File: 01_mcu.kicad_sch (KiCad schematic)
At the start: 3 parts, among them J4 UART, J5 SWD

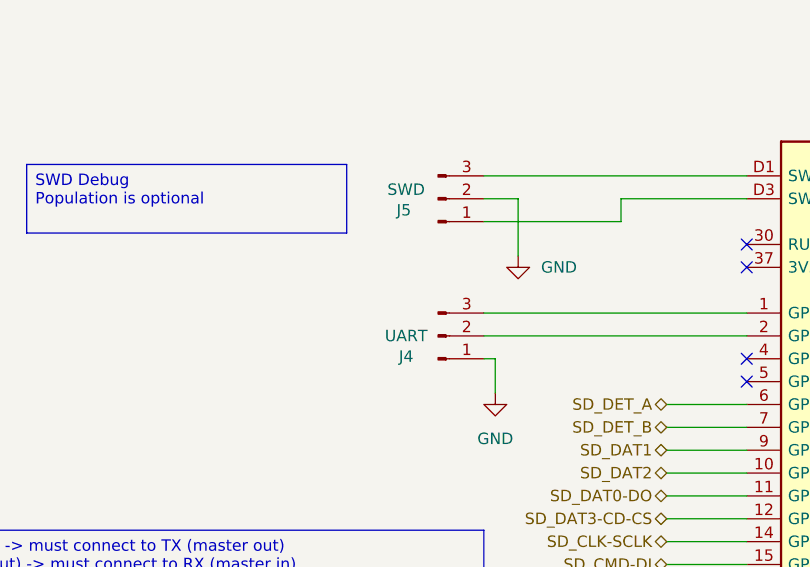
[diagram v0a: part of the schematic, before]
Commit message: Connect both USB data lines again, checked everything with datasheets again
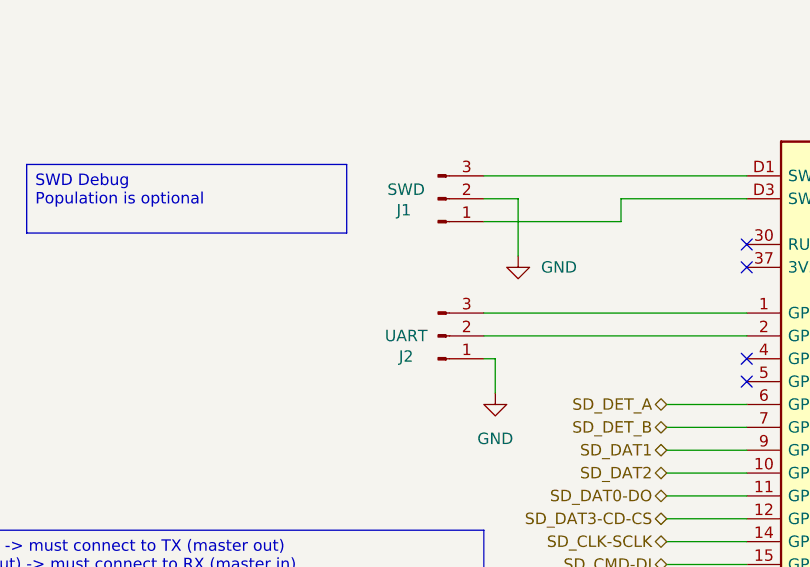
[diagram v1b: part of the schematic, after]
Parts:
- renumbered J5 to J1, J4 to J2
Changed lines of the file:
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@@
 		(dnp no)
 		(fields_autoplaced yes)
-		(property "Reference" "#PWR014"
+		(property "Reference" "#PWR07"
 			(at 158.75 146.05 0)
 			(effects
@@
 			(project ""
 				(path "/ec954637-2a8b-4662-b4a1-f88107f11cb0/8ebc337b-62e9-431a-9c7d-4f5ee75e8f92"
-					(reference "#PWR014")
+					(reference "#PWR07")
 					(unit 1)
 				)
@@
 		(on_board yes)
 		(dnp no)
-		(property "Reference" "J5"
+		(property "Reference" "J1"
 			(at 97.79 71.12 0)
 			(effects
@@
 			(project "ZEReader-Pico"
 				(path "/ec954637-2a8b-4662-b4a1-f88107f11cb0/8ebc337b-62e9-431a-9c7d-4f5ee75e8f92"
-					(reference "J5")
+					(reference "J1")
 					(unit 1)
 				)
@@
 		(on_board yes)
 		(dnp no)
-		(property "Reference" "J4"
+		(property "Reference" "J2"
 			(at 98.044 87.376 0)
 			(effects
@@
 			(project ""
 				(path "/ec954637-2a8b-4662-b4a1-f88107f11cb0/8ebc337b-62e9-431a-9c7d-4f5ee75e8f92"
-					(reference "J4")
+					(reference "J2")
 					(unit 1)
 				)
@@
 		(dnp no)
 		(fields_autoplaced yes)
-		(property "Reference" "#PWR022"
+		(property "Reference" "#PWR06"
 			(at 110.49 82.55 0)
 			(effects
@@
 			(project ""
 				(path "/ec954637-2a8b-4662-b4a1-f88107f11cb0/8ebc337b-62e9-431a-9c7d-4f5ee75e8f92"
-					(reference "#PWR022")
+					(reference "#PWR06")
 					(unit 1)
 				)
@@
 		(dnp no)
 		(fields_autoplaced yes)
-		(property "Reference" "#PWR012"
+		(property "Reference" "#PWR05"
 			(at 107.95 97.79 0)
 			(effects
@@
 			(project ""
 				(path "/ec954637-2a8b-4662-b4a1-f88107f11cb0/8ebc337b-62e9-431a-9c7d-4f5ee75e8f92"
-					(reference "#PWR012")
+					(reference "#PWR05")
 					(unit 1)
 				)
@@
 		(on_board yes)
 		(dnp no)
-		(property "Reference" "#PWR027"
+		(property "Reference" "#PWR08"
 			(at 163.83 41.91 0)
 			(effects
@@
 			(project ""
 				(path "/ec954637-2a8b-4662-b4a1-f88107f11cb0/8ebc337b-62e9-431a-9c7d-4f5ee75e8f92"
-					(reference "#PWR027")
-					(unit 1)
-				)
+					(reference "#PWR08")
+					(unit 1)
+				)

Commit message: Reworked the PCB after review
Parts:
- removed J1: SWD, Connector_PinHeader_2.54mm:PinHeader_1x03_P2.54mm_Vertical, symbol Connector:Conn_01x03_Pin
- added J2: Conn_02x05_Odd_Even, Connector_PinHeader_1.27mm:PinHeader_2x05_P1.27mm_Vertical_SMD, symbol Connector_Generic:Conn_02x05_Odd_Even
- renumbered J2 to J1
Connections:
- net GND: now also J2.3 (Pin_3), J2.5 (Pin_5), J2.9 (Pin_9)
- net at A1.D3 (SWDIO): now also J2.2 (Pin_2)
- net at A1.D1 (SWCLK): now also J2.4 (Pin_4)
- net SD_DET_A: no longer names the net of A1.6 (GPIO4)
- no-connect marks 12 -> 18
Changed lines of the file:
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@@
 	(text_box "SWD Debug\nPopulation is optional"
 		(exclude_from_sim no)
-		(at 55.88 66.04 0)
+		(at 52.07 62.23 0)
 		(size 35.56 7.62)
 		(margins 0.9525 0.9525 0.9525 0.9525)
@@
 			(justify left top)
 		)
+	)
+	(junction
+		(at 92.71 69.85)
+		(diameter 0)
+		(color 0 0 0 0)
+	)
+	(junction
+		(at 92.71 74.93)
+		(diameter 0)
+		(color 0 0 0 0)
 	)
 	(junction
@@
 	)
 	(no_connect
+		(at 135.89 92.71)
+	)
+	(no_connect
+		(at 111.76 69.85)
+	)
+	(no_connect
+		(at 111.76 74.93)
+	)
+	(no_connect
 		(at 135.89 125.73)
 	)
 	(no_connect
+		(at 99.06 72.39)
+	)
+	(no_connect
 		(at 135.89 90.17)
 	)
 	(no_connect
+		(at 99.06 64.77)
+	)
+	(no_connect
 		(at 135.89 74.93)
 	)
@@
 	)
 	(no_connect
+		(at 111.76 72.39)
+	)
+	(no_connect
 		(at 135.89 77.47)
 	)
@@
 	(wire
 		(pts
+			(xy 99.06 69.85) (xy 92.71 69.85)
+		)
+		(stroke
+			(width 0)
+			(type default)
+		)
+	)
+	(wire
+		(pts
 			(xy 181.61 115.57) (xy 189.23 115.57)
 		)
@@
 	(wire
 		(pts
-			(xy 110.49 76.2) (xy 110.49 69.85)
+			(xy 92.71 77.47) (xy 92.71 74.93)
+		)
+		(stroke
+			(width 0)
+			(type default)
+		)
+	)
+	(wire
+		(pts
+			(xy 92.71 69.85) (xy 92.71 67.31)
 		)
 		(stroke
@@
 	(wire
 		(pts
-			(xy 106.68 72.39) (xy 121.92 72.39)
+			(xy 135.89 67.31) (xy 111.76 67.31)
 		)
 		(stroke
@@
 	(wire
 		(pts
-			(xy 106.68 67.31) (xy 135.89 67.31)
-		)
-		(stroke
-			(width 0)
-			(type default)
-		)
-	)
-	(wire
-		(pts
 			(xy 181.61 69.85) (xy 190.5 69.85)
 		)
@@
 	(wire
 		(pts
+			(xy 99.06 67.31) (xy 92.71 67.31)
+		)
+		(stroke
+			(width 0)
+			(type default)
+		)
+	)
+	(wire
+		(pts
 			(xy 163.83 45.72) (xy 163.83 59.69)
 		)
@@
 	(wire
 		(pts
-			(xy 110.49 69.85) (xy 106.68 69.85)
-		)
-		(stroke
-			(width 0)
-			(type default)
-		)
-	)
-	(wire
-		(pts
 			(xy 127 115.57) (xy 135.89 115.57)
 		)
@@
 	(wire
 		(pts
+			(xy 92.71 69.85) (xy 92.71 74.93)
+		)
+		(stroke
+			(width 0)
+			(type default)
+		)
+	)
+	(wire
+		(pts
 			(xy 153.67 38.1) (xy 153.67 59.69)
 		)
@@
 	(wire
 		(pts
-			(xy 127 92.71) (xy 135.89 92.71)
+			(xy 92.71 74.93) (xy 99.06 74.93)
 		)
 		(stroke
@@
 	(wire
 		(pts
-			(xy 121.92 69.85) (xy 121.92 72.39)
+			(xy 111.76 64.77) (xy 121.92 64.77)
+		)
+		(stroke
+			(width 0)
+			(type default)
+		)
+	)
+	(wire
+		(pts
+			(xy 121.92 64.77) (xy 121.92 69.85)
 		)
 		(stroke
@@
 		(shape input)
 		(at 127 118.11 180)
-		(effects
-			(font
-				(size 1.27 1.27)
-			)
-			(justify right)
-		)
-	)
-	(hierarchical_label "SD_DET_A"
-		(shape bidirectional)
-		(at 127 92.71 180)
 		(effects
 			(font
@@
 	(symbol
 		(lib_id "Connector:Conn_01x03_Pin")
-		(at 101.6 69.85 0)
+		(at 101.6 85.09 0)
 		(mirror x)
 		(unit 1)
@@
 		(dnp no)
 		(property "Reference" "J1"
-			(at 97.79 71.12 0)
-			(effects
-				(font
-					(size 1.27 1.27)
-				)
-			)
-		)
-		(property "Value" "SWD"
-			(at 98.044 68.834 0)
-			(effects
-				(font
-					(size 1.27 1.27)
-				)
-			)
-		)
-		(property "Footprint" "Connector_PinHeader_2.54mm:PinHeader_1x03_P2.54mm_Vertical"
-			(at 101.6 69.85 0)
-			(effects
-				(font
-					(size 1.27 1.27)
-				)
-				(hide yes)
-			)
-		)
-		(property "Datasheet" "~"
-			(at 101.6 69.85 0)
-			(effects
-				(font
-					(size 1.27 1.27)
-				)
-				(hide yes)
-			)
-		)
-		(property "Description" "Generic connector, single row, 01x03, script generated"
-			(at 101.6 69.85 0)
-			(effects
-				(font
-					(size 1.27 1.27)
-				)
-				(hide yes)
-			)
-		)
-		(pin "1"
-		)
-		(pin "3"
-		)
-		(pin "2"
-		)
-		(instances
-			(project "ZEReader-Pico"
-				(path "/ec954637-2a8b-4662-b4a1-f88107f11cb0/8ebc337b-62e9-431a-9c7d-4f5ee75e8f92"
-					(reference "J1")
-					(unit 1)
-				)
-			)
-		)
-	)
-	(symbol
-		(lib_id "Connector:Conn_01x03_Pin")
-		(at 101.6 85.09 0)
-		(mirror x)
-		(unit 1)
-		(exclude_from_sim no)
-		(in_bom yes)
-		(on_board yes)
-		(dnp no)
-		(property "Reference" "J2"
 			(at 98.044 87.376 0)
 			(effects
@@
 			(project ""
 				(path "/ec954637-2a8b-4662-b4a1-f88107f11cb0/8ebc337b-62e9-431a-9c7d-4f5ee75e8f92"
-					(reference "J2")
+					(reference "J1")
 					(unit 1)
 				)
@@
 	)
 	(symbol
-		(lib_id "power:GND")
-		(at 110.49 76.2 0)
+		(lib_id "Connector_Generic:Conn_02x05_Odd_Even")
+		(at 104.14 69.85 0)
 		(unit 1)
 		(exclude_from_sim no)
@@
 		(dnp no)
 		(fields_autoplaced yes)
-		(property "Reference" "#PWR06"
-			(at 110.49 82.55 0)
-			(effects
-				(font
-					(size 1.27 1.27)
-				)
-				(hide yes)
-			)
-		)
-		(property "Value" "GND"
-			(at 113.03 77.4699 0)
-			(effects
-				(font
-					(size 1.27 1.27)
-				)
-				(justify left)
-			)
-		)
-		(property "Footprint" ""
-			(at 110.49 76.2 0)
-			(effects
-				(font
-					(size 1.27 1.27)
-				)
-				(hide yes)
-			)
-		)
-		(property "Datasheet" ""
-			(at 110.49 76.2 0)
-			(effects
-				(font
-					(size 1.27 1.27)
-				)
-				(hide yes)
-			)
-		)
-		(property "Description" "Power symbol creates a global label with name \"GND\" , ground"
-			(at 110.49 76.2 0)
-			(effects
-				(font
-					(size 1.27 1.27)
-				)
-				(hide yes)
-			)
+		(property "Reference" "J2"
+			(at 105.41 58.42 0)
+			(effects
+				(font
+					(size 1.27 1.27)
+				)
+			)
+		)
+		(property "Value" "Conn_02x05_Odd_Even"
+			(at 105.41 60.96 0)
+			(effects
+				(font
+					(size 1.27 1.27)
+				)
+			)
+		)
+		(property "Footprint" "Connector_PinHeader_1.27mm:PinHeader_2x05_P1.27mm_Vertical_SMD"
+			(at 104.14 69.85 0)
+			(effects
+				(font
+					(size 1.27 1.27)
+				)
+				(hide yes)
+			)
+		)
+		(property "Datasheet" "~"
+			(at 104.14 69.85 0)
+			(effects
+				(font
+					(size 1.27 1.27)
+				)
+				(hide yes)
+			)
+		)
+		(property "Description" "Generic connector, double row, 02x05, odd/even pin numbering scheme (row 1 odd numbers, row 2 even numbers), script generated (kicad-library-utils/schlib/autogen/connector/)"
+			(at 104.14 69.85 0)
+			(effects
+				(font
+					(size 1.27 1.27)
+				)
+				(hide yes)
+			)
+		)
+		(pin "2"
+		)
+		(pin "4"
+		)
+		(pin "6"
 		)
 		(pin "1"
+		)
+		(pin "5"
+		)
+		(pin "3"
+		)
+		(pin "10"
+		)
+		(pin "8"
+		)
+		(pin "7"
+		)
+		(pin "9"
 		)
 		(instances
 			(project ""
 				(path "/ec954637-2a8b-4662-b4a1-f88107f11cb0/8ebc337b-62e9-431a-9c7d-4f5ee75e8f92"
-					(reference "#PWR06")
+					(reference "J2")
+					(unit 1)
+				)
+			)
+		)
+	)
+	(symbol
+		(lib_id "power:GND")
+		(at 92.71 77.47 0)
+		(unit 1)
+		(exclude_from_sim no)
+		(in_bom yes)
+		(on_board yes)
+		(dnp no)
+		(fields_autoplaced yes)
+		(property "Reference" "#PWR05"
+			(at 92.71 83.82 0)
+			(effects
+				(font
+					(size 1.27 1.27)
+				)
+				(hide yes)
+			)
+		)
+		(property "Value" "GND"
+			(at 95.25 78.7399 0)
+			(effects
+				(font
+					(size 1.27 1.27)
+				)
+				(justify left)
+			)
+		)
+		(property "Footprint" ""
+			(at 92.71 77.47 0)
+			(effects
+				(font
+					(size 1.27 1.27)
+				)
+				(hide yes)
+			)
+		)
+		(property "Datasheet" ""
+			(at 92.71 77.47 0)
+			(effects
+				(font
+					(size 1.27 1.27)
+				)
+				(hide yes)
+			)
+		)
+		(property "Description" "Power symbol creates a global label with name \"GND\" , ground"
+			(at 92.71 77.47 0)
+			(effects
+				(font
+					(size 1.27 1.27)
+				)
+				(hide yes)
+			)
+		)
+		(pin "1"
+		)
+		(instances
+			(project ""
+				(path "/ec954637-2a8b-4662-b4a1-f88107f11cb0/8ebc337b-62e9-431a-9c7d-4f5ee75e8f92"
+					(reference "#PWR05")
 					(unit 1)
 				)
@@
 		(dnp no)
 		(fields_autoplaced yes)
-		(property "Reference" "#PWR05"
+		(property "Reference" "#PWR06"
 			(at 107.95 97.79 0)
 			(effects
@@
 			(project ""
 				(path "/ec954637-2a8b-4662-b4a1-f88107f11cb0/8ebc337b-62e9-431a-9c7d-4f5ee75e8f92"
-					(reference "#PWR05")
+					(reference "#PWR06")
 					(unit 1)
 				)

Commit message: Bigger Zener, improved BoM, general improvements
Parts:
- A1: DigiKey (none) -> 2648-SC1631CT-ND; Manufacturer PartNo (none) -> SC1631
- J1: DigiKey (none) -> 664-G800W305018EU-ND; Manufacturer PartNo (none) -> G800W305018EU
- J2: DigiKey (none) -> 2073-BD125-10-A-0305-0580-L-BCT-ND; Manufacturer PartNo (none) -> BD125-10-A-0305-0580-L-B
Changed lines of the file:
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@@
 			)
 		)
-		(property "Datasheet" "~"
-			(at 101.6 85.09 0)
-			(effects
-				(font
-					(size 1.27 1.27)
-				)
-				(hide yes)
-			)
-		)
-		(property "Description" "Generic connector, single row, 01x03, script generated"
+		(property "Datasheet" "https://cdn.amphenol-cs.com/media/wysiwyg/files/documentation/datasheet/boardwiretoboard/bwb_agilbrick_2_54mm_btb_header_g800.pdf"
+			(at 101.6 85.09 0)
+			(effects
+				(font
+					(size 1.27 1.27)
+				)
+				(hide yes)
+			)
+		)
+		(property "Description" "Steckverbinder Steckleiste Durchkontaktierung 3 positionen 0,100\" (2,54mm)"
+			(at 101.6 85.09 0)
+			(effects
+				(font
+					(size 1.27 1.27)
+				)
+				(hide yes)
+			)
+		)
+		(property "DATASHEET-URL" ""
+			(at 101.6 85.09 0)
+			(effects
+				(font
+					(size 1.27 1.27)
+				)
+				(hide yes)
+			)
+		)
+		(property "DigiKey" "664-G800W305018EU-ND"
+			(at 101.6 85.09 0)
+			(effects
+				(font
+					(size 1.27 1.27)
+				)
+				(hide yes)
+			)
+		)
+		(property "IR" ""
+			(at 101.6 85.09 0)
+			(effects
+				(font
+					(size 1.27 1.27)
+				)
+				(hide yes)
+			)
+		)
+		(property "Manufacturer PartNo" "G800W305018EU"
+			(at 101.6 85.09 0)
+			(effects
+				(font
+					(size 1.27 1.27)
+				)
+				(hide yes)
+			)
+		)
+		(property "PACKAGING" ""
+			(at 101.6 85.09 0)
+			(effects
+				(font
+					(size 1.27 1.27)
+				)
+				(hide yes)
+			)
+		)
+		(property "PART-NUMBER" ""
+			(at 101.6 85.09 0)
+			(effects
+				(font
+					(size 1.27 1.27)
+				)
+				(hide yes)
+			)
+		)
+		(property "QTY" ""
+			(at 101.6 85.09 0)
+			(effects
+				(font
+					(size 1.27 1.27)
+				)
+				(hide yes)
+			)
+		)
+		(property "VR" ""
 			(at 101.6 85.09 0)
 			(effects
@@
 			)
 		)
-		(property "Datasheet" "https://datasheets.raspberrypi.com/pico/pico-datasheet.pdf"
+		(property "Datasheet" "https://datasheets.raspberrypi.com/pico/pico-2-datasheet.pdf"
 			(at 158.75 147.32 0)
 			(effects
@@
 			)
 		)
-		(property "Description" "Versatile and inexpensive microcontroller module (with full pinout for test point and debug connections) powered by RP2040 dual-core Arm Cortex-M0+ processor up to 133 MHz, 264kB SRAM, 2MB QSPI flash; also supports Raspberry Pi Pico 2"
+		(property "Description" "RP2350 Raspberry Pi Pico 2 - ARM® Cortex®-M33 MCU 32-Bit Evaluierungsboards - Embedded"
 			(at 158.75 149.86 0)
+			(effects
+				(font
+					(size 1.27 1.27)
+				)
+				(hide yes)
+			)
+		)
+		(property "DigiKey" "2648-SC1631CT-ND"
+			(at 158.75 97.79 0)
+			(effects
+				(font
+					(size 1.27 1.27)
+				)
+				(hide yes)
+			)
+		)
+		(property "DATASHEET-URL" ""
+			(at 158.75 97.79 0)
+			(effects
+				(font
+					(size 1.27 1.27)
+				)
+				(hide yes)
+			)
+		)
+		(property "IR" ""
+			(at 158.75 97.79 0)
+			(effects
+				(font
+					(size 1.27 1.27)
+				)
+				(hide yes)
+			)
+		)
+		(property "Manufacturer PartNo" "SC1631"
+			(at 158.75 97.79 0)
+			(effects
+				(font
+					(size 1.27 1.27)
+				)
+				(hide yes)
+			)
+		)
+		(property "PACKAGING" ""
+			(at 158.75 97.79 0)
+			(effects
+				(font
+					(size 1.27 1.27)
+				)
+				(hide yes)
+			)
+		)
+		(property "PART-NUMBER" ""
+			(at 158.75 97.79 0)
+			(effects
+				(font
+					(size 1.27 1.27)
+				)
+				(hide yes)
+			)
+		)
+		(property "QTY" ""
+			(at 158.75 97.79 0)
+			(effects
+				(font
+					(size 1.27 1.27)
+				)
+				(hide yes)
+			)
+		)
+		(property "VR" ""
+			(at 158.75 97.79 0)
 			(effects
 				(font
@@
 			)
 		)
-		(property "Datasheet" "~"
+		(property "Datasheet" "https://gct.co/files/specs/1.27mm-header-spec.pdf"
 			(at 104.14 69.85 0)
 			(effects
@@
 			(at 104.14 69.85 0)
 			(effects
+				(font
+					(size 1.27 1.27)
+				)
+				(hide yes)
+			)
+		)
+		(property "DigiKey" "2073-BD125-10-A-0305-0580-L-BCT-ND"
+			(at 104.14 69.85 0)
+			(effects
+				(font
+					(size 1.27 1.27)
+				)
+				(hide yes)
+			)
+		)
+		(property "DATASHEET-URL" ""
+			(at 104.14 69.85 0)
+			(effects
+				(font
+					(size 1.27 1.27)
+				)
+				(hide yes)
+			)
+		)
+		(property "IR" ""
+			(at 104.14 69.85 0)
+			(effects
+				(font
+					(size 1.27 1.27)
+				)
+				(hide yes)
+			)
+		)
+		(property "Manufacturer PartNo" "BD125-10-A-0305-0580-L-B"
+			(at 104.14 69.85 0)
+			(effects
+				(font
+					(size 1.27 1.27)
+				)
+				(hide yes)
+			)
+		)
+		(property "PACKAGING" ""
+			(at 104.14 69.85 0)
+			(effects
+				(font
+					(size 1.27 1.27)
+				)
+				(hide yes)
+			)
+		)
+		(property "PART-NUMBER" ""
+			(at 104.14 69.85 0)
+			(effects
+				(font
+					(size 1.27 1.27)
+				)
+				(hide yes)
+			)
+		)
+		(property "QTY" ""
+			(at 104.14 69.85 0)
+			(effects
+				(font
+					(size 1.27 1.27)
+				)
+				(hide yes)
+			)
+		)
+		(property "VR" ""
+			(at 104.14 69.85 0)
+			(effects

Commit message: Add proper charging detection, fix zener footprint
Connect the BQ25 status pin to the microcontroller for a proper
charging detection (low active).
Correct the footprint for the selected zener diode.
Somehow, the wrong footprint got assigned.
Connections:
- net CHARGING: now reaches A1.31 (GPIO26_ADC0)
- no-connect marks 18 -> 17
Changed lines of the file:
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@@
 	)
 	(no_connect
-		(at 181.61 110.49)
+		(at 135.89 92.71)
+	)
+	(no_connect
+		(at 111.76 69.85)
+	)
+	(no_connect
+		(at 111.76 74.93)
+	)
+	(no_connect
+		(at 135.89 125.73)
+	)
+	(no_connect
+		(at 99.06 72.39)
+	)
+	(no_connect
+		(at 135.89 90.17)
+	)
+	(no_connect
+		(at 99.06 64.77)
+	)
+	(no_connect
+		(at 135.89 74.93)
+	)
+	(no_connect
+		(at 181.61 105.41)
+	)
+	(no_connect
+		(at 181.61 77.47)
+	)
+	(no_connect
+		(at 111.76 72.39)
+	)
+	(no_connect
+		(at 135.89 77.47)
+	)
+	(no_connect
+		(at 181.61 67.31)
+	)
+	(no_connect
+		(at 181.61 80.01)
+	)
+	(no_connect
+		(at 181.61 120.65)
+	)
+	(no_connect
+		(at 135.89 87.63)
 	)
 	(no_connect
 		(at 181.61 85.09)
 	)
-	(no_connect
-		(at 135.89 92.71)
-	)
-	(no_connect
-		(at 111.76 69.85)
-	)
-	(no_connect
-		(at 111.76 74.93)
-	)
-	(no_connect
-		(at 135.89 125.73)
-	)
-	(no_connect
-		(at 99.06 72.39)
-	)
-	(no_connect
-		(at 135.89 90.17)
-	)
-	(no_connect
-		(at 99.06 64.77)
-	)
-	(no_connect
-		(at 135.89 74.93)
-	)
-	(no_connect
-		(at 181.61 105.41)
-	)
-	(no_connect
-		(at 181.61 77.47)
-	)
-	(no_connect
-		(at 111.76 72.39)
-	)
-	(no_connect
-		(at 135.89 77.47)
-	)
-	(no_connect
-		(at 181.61 67.31)
-	)
-	(no_connect
-		(at 181.61 80.01)
-	)
-	(no_connect
-		(at 181.61 120.65)
-	)
-	(no_connect
-		(at 135.89 87.63)
-	)
 	(wire
 		(pts
@@
 		(pts
 			(xy 135.89 67.31) (xy 111.76 67.31)
+		)
+		(stroke
+			(width 0)
+			(type default)
+		)
+	)
+	(wire
+		(pts
+			(xy 181.61 110.49) (xy 189.23 110.49)
 		)
 		(stroke
@@
 		)
 	)
+	(hierarchical_label "CHARGING"
+		(shape input)
+		(at 189.23 110.49 0)
+		(effects
+			(font
+				(size 1.27 1.27)
+			)
+			(justify left)
+		)
+	)
